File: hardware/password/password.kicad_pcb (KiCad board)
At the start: 2 copper layers, 100 x 100 mm, 73 parts, among them J1 RJ45_Shielded, SW1 SW_DIP_x01, SW10 SW_DIP_x01, SW11 SW_DIP_x01, SW2 SW_DIP_x01, SW3 SW_DIP_x01, SW4 SW_DIP_x01, SW5 SW_DIP_x01, SW6 SW_DIP_x01, SW7 SW_DIP_x01, SW8 SW_DIP_x01, SW9 SW_DIP_x01, U1 WAVGAT_CAN, U2 HT1632C-52LQFP

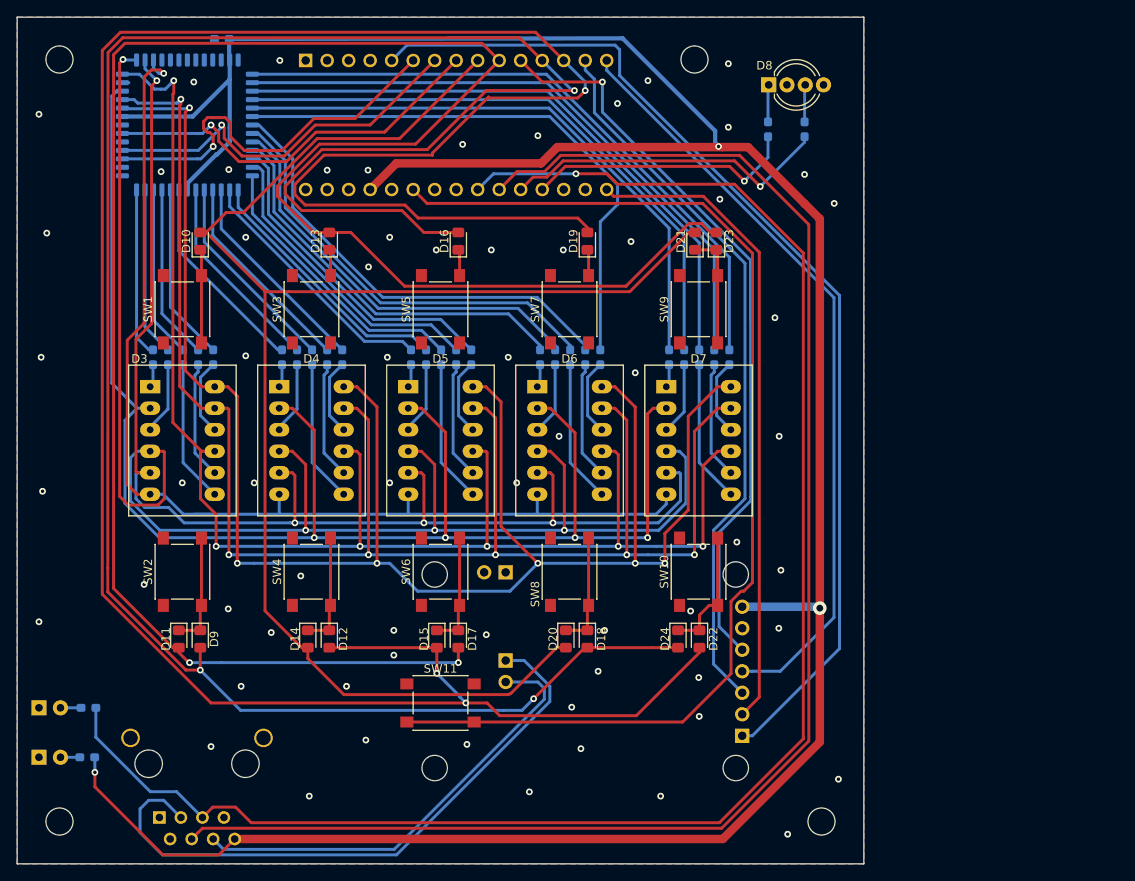
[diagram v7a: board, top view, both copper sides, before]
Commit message: Password PCB: change display polarity
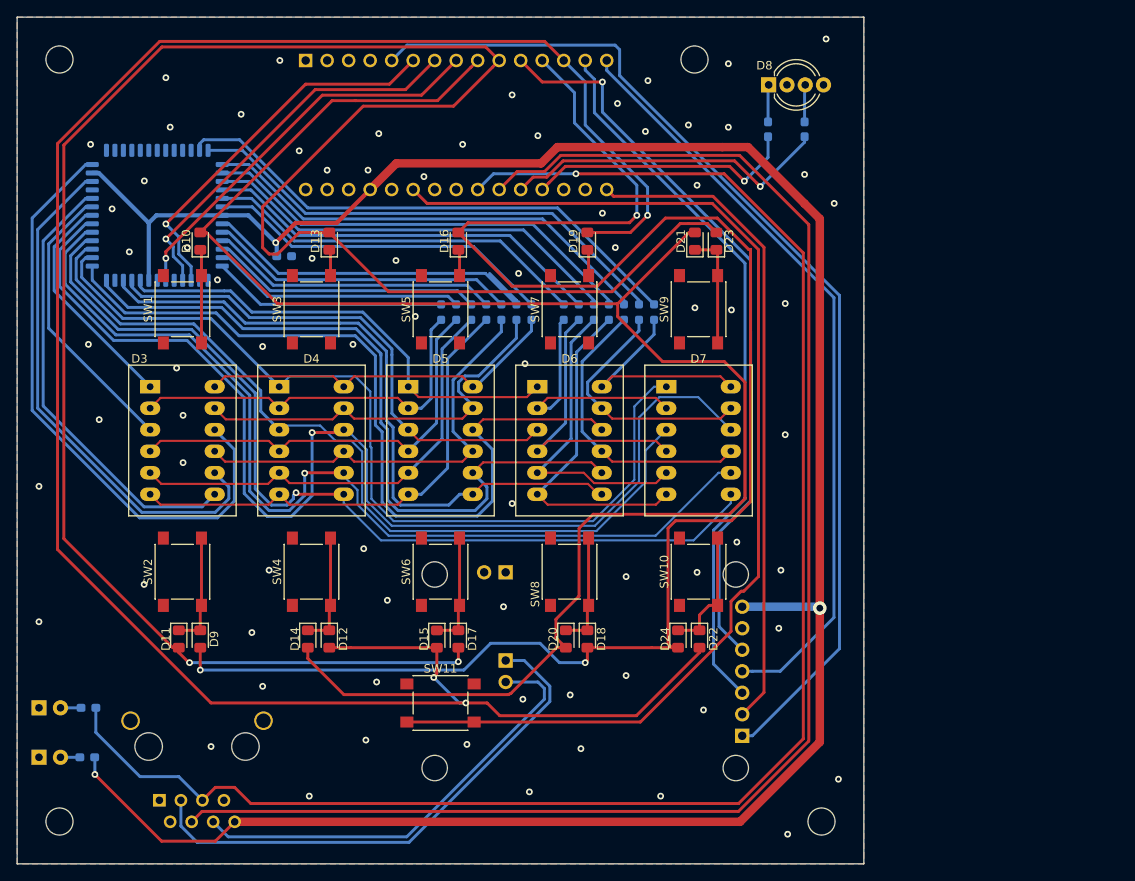
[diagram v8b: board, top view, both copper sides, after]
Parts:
- removed R17, R18, R19, R20, R21, R22, R23, R24, R25, R26, R27: 220R, Resistor_SMD:R_0603_1608Metric_Pad1.05x0.95mm_HandSolder
- R10, R11, R12, R13, R14, R15, R16, R3, R4, R5, R6, R7, R8, R9: value 220R -> 82R; footprint Resistor_SMD:R_0603_1608Metric_Pad1.05x0.95mm_HandSolder -> Resistor_SMD:R_0603_1608Metric_Pad0.98x0.95mm_HandSolder
- R28, R29: value 220R -> 82R
- moved R7 41.5 mm to (107.2, 84.8), turned to 90 degrees
- moved R6 38.0 mm to (105.4, 84.8), turned to 90 degrees
- moved R12 37.2 mm to (118.1, 84.8), turned to 90 degrees
- moved R11 33.7 mm to (116.3, 84.8), turned to 90 degrees
- moved R4 32.7 mm to (101.9, 84.8), turned to 90 degrees
- moved R5 30.9 mm to (103.6, 84.8), turned to 90 degrees
- moved R3 29.2 mm to (100.1, 84.8), turned to 90 degrees
- moved R16 27.4 mm to (125.2, 84.8), turned to 90 degrees
- moved R10 26.7 mm to (114.6, 84.8), turned to 90 degrees
- moved C1 26.7 mm to (81.5, 78.2), turned to 180 degrees
- moved R9 26.5 mm to (110.7, 84.8), turned to 90 degrees
- moved R8 23.0 mm to (109.0, 84.8), turned to 90 degrees
- moved R14 22.2 mm to (121.7, 84.8), turned to 90 degrees
- moved R15 20.5 mm to (123.4, 84.8), turned to 90 degrees
- moved R13 18.8 mm to (119.9, 84.8), turned to 90 degrees
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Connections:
- D3 pad 1: Net-(D3-Pad1) -> /COL1
- D3 pad 10: Net-(D3-Pad10) -> /COL3
- D3 pad 11: Net-(D3-Pad11) -> /ROW2L
- D3 pad 12: Net-(D3-Pad12) -> /ROW1L
- D3 pad 2: Net-(D3-Pad2) -> /ROW3L
- D3 pad 3: Net-(D3-Pad3) -> /COL2
- D3 pad 4: Net-(D3-Pad4) -> /ROW5L
- D3 pad 5: Net-(D3-Pad5) -> /ROW6L
- D3 pad 6: Net-(D3-Pad6) -> /ROW7L
- D3 pad 7: Net-(D3-Pad7) -> /COL4
- D3 pad 8: Net-(D3-Pad8) -> /COL5
- D3 pad 9: Net-(D3-Pad9) -> /ROW4L
- D4 pad 1: Net-(D4-Pad1) -> /COL6
- D4 pad 10: Net-(D4-Pad10) -> /COL8
- D4 pad 11: Net-(D3-Pad11) -> /ROW2L
- D4 pad 12: Net-(D3-Pad12) -> /ROW1L
- D4 pad 2: Net-(D3-Pad2) -> /ROW3L
- D4 pad 3: Net-(D4-Pad3) -> /COL7
- D4 pad 4: Net-(D3-Pad4) -> /ROW5L
- D4 pad 5: Net-(D3-Pad5) -> /ROW6L
- D4 pad 6: Net-(D3-Pad6) -> /ROW7L
- D4 pad 7: Net-(D4-Pad7) -> /COL9
- D4 pad 8: Net-(D4-Pad8) -> /COL10
- D4 pad 9: Net-(D3-Pad9) -> /ROW4L
- D5 pad 1: Net-(D5-Pad1) -> /COL11
- D5 pad 10: Net-(D5-Pad10) -> /COL13
- D5 pad 11: Net-(D3-Pad11) -> /ROW2L
- D5 pad 12: Net-(D3-Pad12) -> /ROW1L
- D5 pad 2: Net-(D3-Pad2) -> /ROW3L
- D5 pad 3: Net-(D5-Pad3) -> /COL12
- D5 pad 4: Net-(D3-Pad4) -> /ROW5L
- D5 pad 5: Net-(D3-Pad5) -> /ROW6L
- D5 pad 6: Net-(D3-Pad6) -> /ROW7L
- D5 pad 7: Net-(D5-Pad7) -> /COL14
- D5 pad 8: Net-(D5-Pad8) -> /COL15
- D5 pad 9: Net-(D3-Pad9) -> /ROW4L
- D6 pad 1: Net-(D6-Pad1) -> /COL11
- D6 pad 10: Net-(D6-Pad10) -> /COL13
- D6 pad 11: Net-(D3-Pad11) -> /ROW2R
- D6 pad 12: Net-(D3-Pad12) -> /ROW1R
- D6 pad 2: Net-(D3-Pad2) -> /ROW3R
- D6 pad 3: Net-(D6-Pad3) -> /COL12
- D6 pad 4: Net-(D3-Pad4) -> /ROW5R
- D6 pad 5: Net-(D3-Pad5) -> /ROW6R
- D6 pad 6: Net-(D3-Pad6) -> /ROW7R
- D6 pad 7: Net-(D6-Pad7) -> /COL14
- D6 pad 8: Net-(D6-Pad8) -> /COL15
- D6 pad 9: Net-(D3-Pad9) -> /ROW4R
- D7 pad 1: Net-(D7-Pad1) -> /COL6
- D7 pad 10: Net-(D7-Pad10) -> /COL8
- D7 pad 11: Net-(D3-Pad11) -> /ROW2R
- D7 pad 12: Net-(D3-Pad12) -> /ROW1R
- D7 pad 2: Net-(D3-Pad2) -> /ROW3R
- D7 pad 3: Net-(D7-Pad3) -> /COL7
- D7 pad 4: Net-(D3-Pad4) -> /ROW5R
- D7 pad 5: Net-(D3-Pad5) -> /ROW6R
- D7 pad 6: Net-(D3-Pad6) -> /ROW7R
- D7 pad 7: Net-(D7-Pad7) -> /COL9
- D7 pad 8: Net-(D7-Pad8) -> /COL10
- D7 pad 9: Net-(D3-Pad9) -> /ROW4R
- R10 pad 1: Net-(R10-Pad1) -> /ROW3R
- R10 pad 2: Net-(D4-Pad10) -> Net-(R10-Pad2)
- R11 pad 1: Net-(R11-Pad1) -> /ROW5R
- R11 pad 2: Net-(D4-Pad3) -> Net-(R11-Pad2)
- R12 pad 1: Net-(R12-Pad1) -> /ROW6R
- R12 pad 2: Net-(D4-Pad1) -> Net-(R12-Pad2)
- R13 pad 1: Net-(R13-Pad1) -> /ROW7R
- R13 pad 2: Net-(D5-Pad8) -> Net-(R13-Pad2)
- R14 pad 1: Net-(R14-Pad1) -> /ROW4R
- R14 pad 2: Net-(D5-Pad7) -> Net-(R14-Pad2)
- R15 pad 1: Net-(R15-Pad1) -> /ROW2R
- R15 pad 2: Net-(D5-Pad10) -> Net-(R15-Pad2)
- R16 pad 1: Net-(R16-Pad1) -> /ROW1R
- R16 pad 2: Net-(D5-Pad3) -> Net-(R16-Pad2)
- R3 pad 1: Net-(R3-Pad1) -> /ROW3L
- R3 pad 2: Net-(D3-Pad8) -> Net-(R3-Pad2)
- R4 pad 1: Net-(R4-Pad1) -> /ROW5L
- R4 pad 2: Net-(D3-Pad7) -> Net-(R4-Pad2)
- R5 pad 1: Net-(R5-Pad1) -> /ROW6L
- R5 pad 2: Net-(D3-Pad10) -> Net-(R5-Pad2)
- R6 pad 1: Net-(R6-Pad1) -> /ROW7L
- R6 pad 2: Net-(D3-Pad3) -> Net-(R6-Pad2)
- R7 pad 1: Net-(R7-Pad1) -> /ROW4L
- R7 pad 2: Net-(D3-Pad1) -> Net-(R7-Pad2)
- R8 pad 1: Net-(R8-Pad1) -> /ROW2L
- R8 pad 2: Net-(D4-Pad8) -> Net-(R8-Pad2)
- R9 pad 1: Net-(R9-Pad1) -> /ROW1L
- R9 pad 2: Net-(D4-Pad7) -> Net-(R9-Pad2)
- U2 pad 1: Net-(R16-Pad1) -> Net-(R14-Pad2)
- U2 pad 10: Net-(R3-Pad1) -> Net-(R6-Pad2)
- U2 pad 11: Net-(R4-Pad1) -> Net-(R5-Pad2)
- U2 pad 12: Net-(R6-Pad1) -> Net-(R4-Pad2)
- U2 pad 13: Net-(R7-Pad1) -> Net-(R3-Pad2)
- U2 pad 2: Net-(R17-Pad1) -> Net-(R13-Pad2)
- U2 pad 22: Net-(D3-Pad12) -> /COL11
- U2 pad 23: Net-(D3-Pad11) -> /COL12
- U2 pad 24: Net-(D3-Pad2) -> /COL14
- U2 pad 26: Net-(D3-Pad9) -> /COL15
- U2 pad 27: Net-(D3-Pad4) -> /COL13
- U2 pad 28: Net-(D3-Pad5) -> /COL6
- U2 pad 29: Net-(D3-Pad6) -> /COL7
- U2 pad 3: Net-(R10-Pad1) -> Net-(R12-Pad2)
- U2 pad 30: Net-(U2-Pad30) -> /COL9
- U2 pad 31: Net-(U2-Pad31) -> /COL10
- U2 pad 32: Net-(U2-Pad32) -> /COL8
- U2 pad 33: Net-(U2-Pad33) -> /COL1
- U2 pad 34: Net-(U2-Pad34) -> /COL2
- U2 pad 35: Net-(U2-Pad35) -> /COL4
- U2 pad 37: Net-(U2-Pad37) -> /COL5
- U2 pad 39: Net-(U2-Pad39) -> /COL3
- U2 pad 4: Net-(R8-Pad1) -> Net-(R11-Pad2)
- U2 pad 5: Net-(R9-Pad1) -> Net-(R10-Pad2)
- U2 pad 50: Net-(R15-Pad1) -> Net-(U2-Pad50)
- U2 pad 51: Net-(R13-Pad1) -> Net-(R16-Pad2)
- U2 pad 52: Net-(R14-Pad1) -> Net-(R15-Pad2)
- U2 pad 6: Net-(R11-Pad1) -> Net-(R9-Pad2)
- U2 pad 8: Net-(R12-Pad1) -> Net-(R8-Pad2)
- U2 pad 9: Net-(R5-Pad1) -> Net-(R7-Pad2)
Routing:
- net Net-(D3-Pad12): track 216.3 -> 0.00 mm, vias 6 -> 0
- net Net-(D3-Pad11): track 198.7 -> 0.00 mm, vias 6 -> 0
- net Net-(D3-Pad2): track 187.4 -> 0.00 mm, vias 4 -> 0
- net Net-(D3-Pad4): track 185.4 -> 0.00 mm, vias 4 -> 0
- net Net-(D3-Pad9): track 175.7 -> 0.00 mm, vias 6 -> 0
- net Net-(D3-Pad5): track 150.9 -> 0.00 mm, vias 4 -> 0
- net /COL8: track 0.00 -> 135.8 mm, vias 0 -> 1
- net Net-(D3-Pad6): track 130.2 -> 0.00 mm, vias 1 -> 0
- net /COL10: track 0.00 -> 115.0 mm, vias 0 -> 1
- net /COL9: track 0.00 -> 108.5 mm, vias 0 -> 1
- net /COL6: track 0.00 -> 104.3 mm
- net /COL7: track 0.00 -> 99.3 mm
- net /COL13: track 0.00 -> 96.5 mm
- net /COL15: track 0.00 -> 86.9 mm
- net /COL14: track 0.00 -> 79.2 mm
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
